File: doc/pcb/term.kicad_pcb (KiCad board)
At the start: 2 copper layers, 102.8 x 75.6 mm, 18 parts, among them U1 LM35-LP, U2 LM1117-3.3, U3 STM32F030F4Px, U4 CA56-12CGKWA

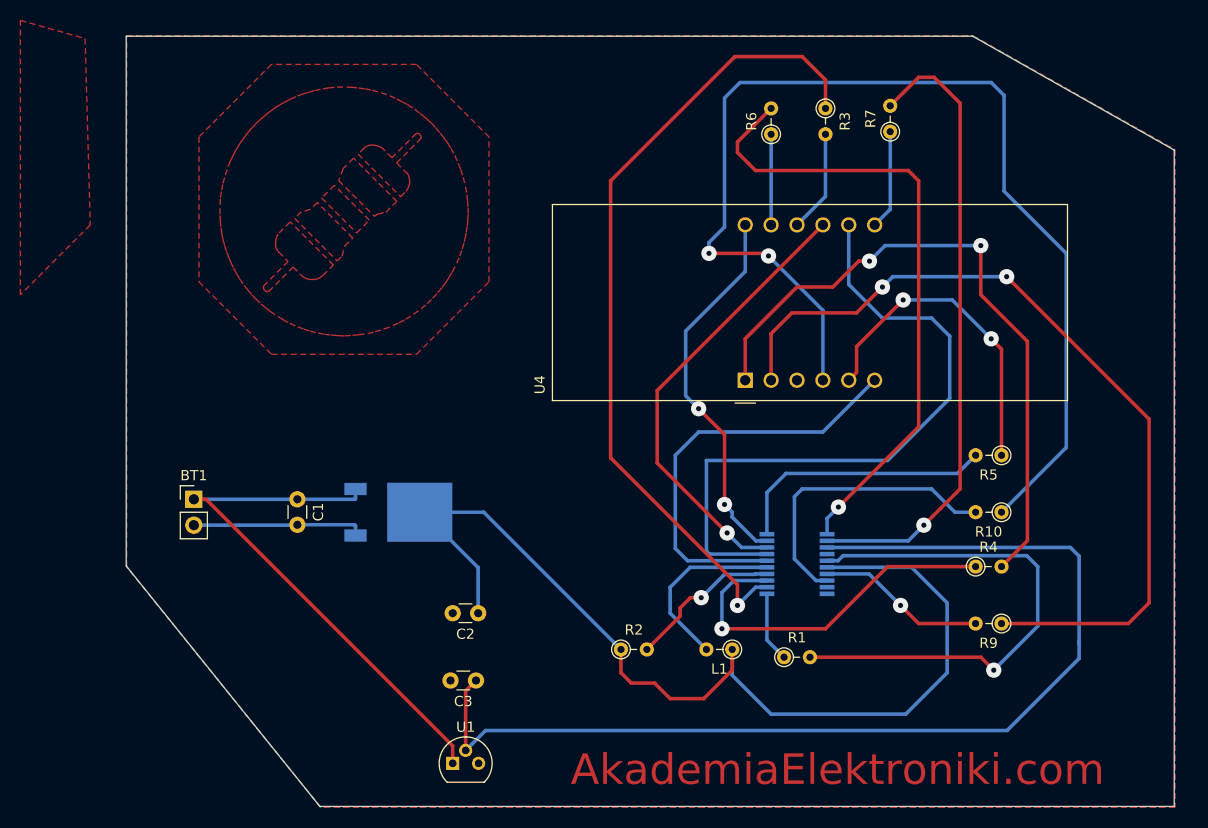
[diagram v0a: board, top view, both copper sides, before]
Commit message: new pcb as credit card
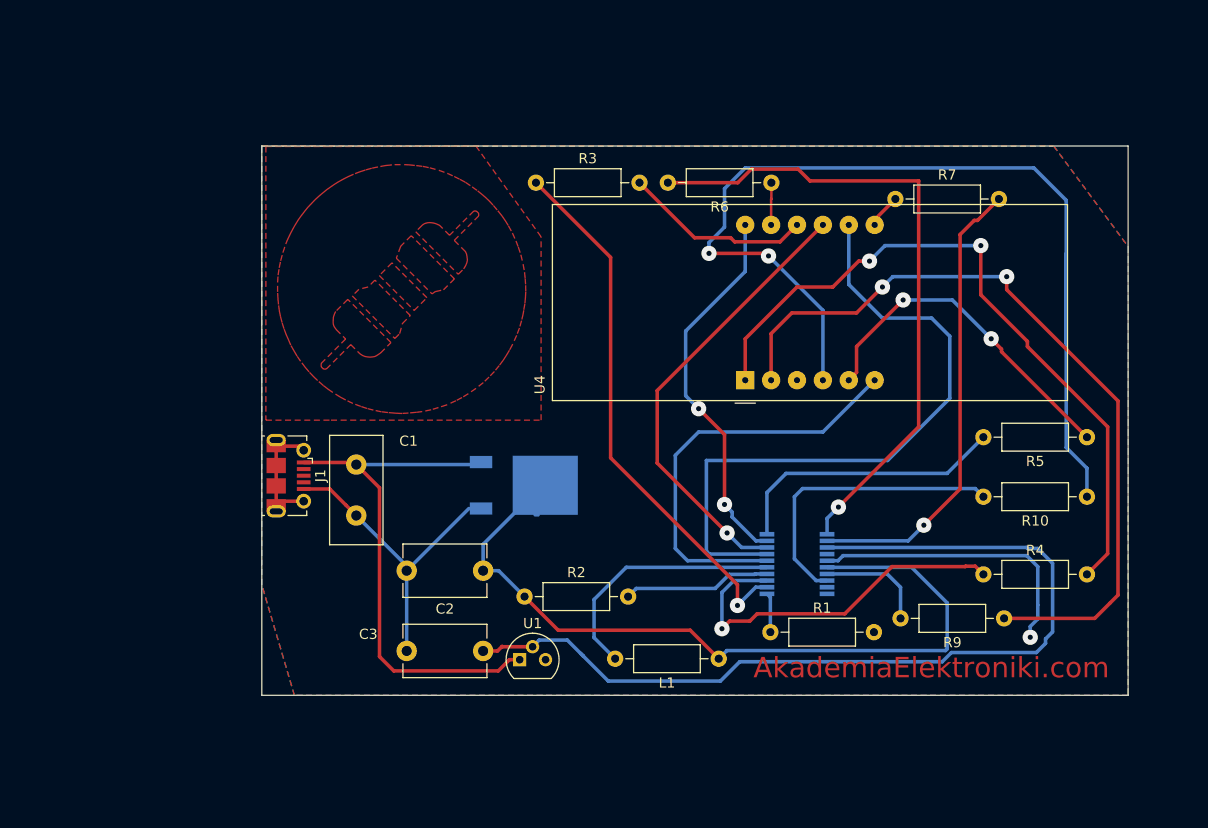
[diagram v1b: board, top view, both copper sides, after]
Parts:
- removed BT1: Battery, Connector_PinHeader_2.54mm:PinHeader_1x02_P2.54mm_Vertical
- added J1: USB_B_Micro, Connector_USB:USB_Micro-B_Molex-105017-0001, F.Cu at (138.3, 103.3)
- C1: footprint Capacitor_THT:C_Disc_D3.0mm_W1.6mm_P2.50mm -> Capacitor_THT:C_Disc_D10.5mm_W5.0mm_P5.00mm
- C2, C3: footprint Capacitor_THT:C_Disc_D3.0mm_W1.6mm_P2.50mm -> Capacitor_THT:C_Disc_D8.0mm_W5.0mm_P7.50mm
- L1, R1, R10, R2, R3, R4, R5, R6, R7, R9: footprint Resistor_THT:R_Axial_DIN0204_L3.6mm_D1.6mm_P2.54mm_Vertical -> Resistor_THT:R_Axial_DIN0207_L6.3mm_D2.5mm_P10.16mm_Horizontal
- moved R3 29.3 mm to (162.6, 74.6), turned to 0 degrees
- moved U2 12.6 mm to (161.4, 104.3)
- moved U1 12.1 mm to (161.0, 121.4)
- moved R2 10.8 mm to (161.5, 115.2)
- moved R5 8.57 mm to (216.7, 99.6)
- moved R10 8.52 mm to (216.7, 105.4)
- moved C1 6.71 mm to (145.0, 102.3)
- moved R7 6.62 mm to (197.9, 76.2), turned to 0 degrees
- moved R6 4.75 mm to (185.7, 74.6), turned to 180 degrees
- moved C2 4.20 mm to (157.4, 112.7)
- moved C3 2.98 mm to (157.4, 120.5)
- moved R1 2.80 mm to (185.6, 118.7)
- moved L1 1.61 mm to (180.5, 121.3)
- moved R4 1.08 mm to (206.5, 113.0)
- moved R9 0.57 mm to (208.5, 117.3)
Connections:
- net +9V renamed +5V
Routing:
- net Net-(R3-Pad1): track 80.3 -> 53.3 mm
- net Net-(C2-Pad1): track 102.2 -> 78.3 mm
- net Net-(R7-Pad2): track 62.1 -> 45.4 mm
- net Net-(C3-Pad1): track 106.6 -> 90.1 mm
- net Net-(J1-Pad6): track 0.00 -> 12.9 mm
- net GND: track 68.7 -> 58.3 mm
- net SF: track 10.0 -> 18.5 mm
- net Net-(L1-Pad2): track 17.9 -> 24.9 mm
- net SB: track 9.78 -> 3.38 mm
- net Net-(R9-Pad2): track 16.6 -> 10.8 mm, vias 1 -> 0
- net SD: track 83.1 -> 77.9 mm
- net SA: track 8.89 -> 4.51 mm
- net SC: track 110.9 -> 106.9 mm
- net SE: track 65.4 -> 69.2 mm
- net Net-(R1-Pad1): track 6.91 -> 3.90 mm
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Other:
- board size 102.8 x 75.6 mm -> 85 x 53.9 mm

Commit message: little details
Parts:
- R10: moved to B.Cu
- moved R7 1.96 mm to (198.4, 74.3)
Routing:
- net SG: track 33.8 -> 40.3 mm
- net SB: track 3.38 -> 5.49 mm
- net Net-(R7-Pad2): track 45.4 -> 47.3 mm
- net Net-(R6-Pad2): track 64.0 -> 65.6 mm
- net SE: track 69.2 -> 69.9 mm

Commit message: little pcb corrections
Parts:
- J1: footprint Connector_USB:USB_Micro-B_Molex-105017-0001 -> Connector_USB:USB_Micro-B_Molex_47346-0001
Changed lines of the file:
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@@
     (thickness 1.6)
     (drawings 8)
-    (tracks 233)
+    (tracks 232)
     (zones 0)
     (modules 18)
@@
     )
   )
-  (module Connector_USB:USB_Micro-B_Molex-105017-0001 (layer F.Cu)
+  (module Connector_USB:USB_Micro-B_Molex_47346-0001 (layer F.Cu)
     (at 138.35 103.35 270)
-    (descr http://www.molex.com/pdm_docs/sd/1050170001_sd.pdf)
-    (tags "Micro-USB SMD Typ-B")
+    (descr "Micro USB B receptable with flange, bottom-mount, SMD, right-angle (http://www.molex.com/pdm_docs/sd/473460001_sd.pdf)")
+    (tags "Micro B USB SMD")
     (attr smd)
-    (fp_text reference J1 (at 0 -3.1125 90) (layer F.SilkS)
-      (effects (font (size 1 1) (thickness 0.15)))
-    )
-    (fp_text value USB_B_Micro (at 5.95 -1.35 180) (layer F.Fab)
-      (effects (font (size 1 1) (thickness 0.15)))
-    )
-    (fp_text user "PCB Edge" (at 0 2.6875 90) (layer Dwgs.User)
-      (effects (font (size 0.5 0.5) (thickness 0.08)))
-    )
-    (fp_text user %R (at 0 0.8875 90) (layer F.Fab)
-      (effects (font (size 1 1) (thickness 0.15)))
-    )
-    (fp_line (start -4.4 3.64) (end 4.4 3.64) (layer F.CrtYd) (width 0.05))
-    (fp_line (start 4.4 -2.46) (end 4.4 3.64) (layer F.CrtYd) (width 0.05))
-    (fp_line (start -4.4 -2.46) (end 4.4 -2.46) (layer F.CrtYd) (width 0.05))
-    (fp_line (start -4.4 3.64) (end -4.4 -2.46) (layer F.CrtYd) (width 0.05))
-    (fp_line (start -3.9 -1.7625) (end -3.45 -1.7625) (layer F.SilkS) (width 0.12))
-    (fp_line (start -3.9 0.0875) (end -3.9 -1.7625) (layer F.SilkS) (width 0.12))
-    (fp_line (start 3.9 2.6375) (end 3.9 2.3875) (layer F.SilkS) (width 0.12))
-    (fp_line (start 3.75 3.3875) (end 3.75 -1.6125) (layer F.Fab) (width 0.1))
-    (fp_line (start -3 2.689204) (end 3 2.689204) (layer F.Fab) (width 0.1))
-    (fp_line (start -3.75 3.389204) (end 3.75 3.389204) (layer F.Fab) (width 0.1))
-    (fp_line (start -3.75 -1.6125) (end 3.75 -1.6125) (layer F.Fab) (width 0.1))
-    (fp_line (start -3.75 3.3875) (end -3.75 -1.6125) (layer F.Fab) (width 0.1))
-    (fp_line (start -3.9 2.6375) (end -3.9 2.3875) (layer F.SilkS) (width 0.12))
-    (fp_line (start 3.9 0.0875) (end 3.9 -1.7625) (layer F.SilkS) (width 0.12))
-    (fp_line (start 3.9 -1.7625) (end 3.45 -1.7625) (layer F.SilkS) (width 0.12))
-    (fp_line (start -1.7 -2.3125) (end -1.25 -2.3125) (layer F.SilkS) (width 0.12))
-    (fp_line (start -1.7 -2.3125) (end -1.7 -1.8625) (layer F.SilkS) (width 0.12))
-    (fp_line (start -1.3 -1.7125) (end -1.5 -1.9125) (layer F.Fab) (width 0.1))
-    (fp_line (start -1.1 -1.9125) (end -1.3 -1.7125) (layer F.Fab) (width 0.1))
-    (fp_line (start -1.5 -2.1225) (end -1.1 -2.1225) (layer F.Fab) (width 0.1))
-    (fp_line (start -1.5 -2.1225) (end -1.5 -1.9125) (layer F.Fab) (width 0.1))
-    (fp_line (start -1.1 -2.1225) (end -1.1 -1.9125) (layer F.Fab) (width 0.1))
-    (pad 6 smd rect (at 1 1.2375 270) (size 1.5 1.9) (layers F.Cu F.Paste F.Mask)
+    (fp_text reference J1 (at 0 -3.3 270) (layer F.SilkS)
+      (effects (font (size 1 1) (thickness 0.15)))
+    )
+    (fp_text value USB_B_Micro (at 0 4.6 270) (layer F.Fab)
+      (effects (font (size 1 1) (thickness 0.15)))
+    )
+    (fp_text user "PCB Edge" (at 0 2.67 270) (layer Dwgs.User)
+      (effects (font (size 0.4 0.4) (thickness 0.04)))
+    )
+    (fp_text user %R (at 0 1.2 90) (layer F.Fab)
+      (effects (font (size 1 1) (thickness 0.15)))
+    )
+    (fp_line (start 3.81 -1.71) (end 3.43 -1.71) (layer F.SilkS) (width 0.12))
+    (fp_line (start 4.6 3.9) (end -4.6 3.9) (layer F.CrtYd) (width 0.05))
+    (fp_line (start 4.6 -2.7) (end 4.6 3.9) (layer F.CrtYd) (width 0.05))
+    (fp_line (start -4.6 -2.7) (end 4.6 -2.7) (layer F.CrtYd) (width 0.05))
+    (fp_line (start -4.6 3.9) (end -4.6 -2.7) (layer F.CrtYd) (width 0.05))
+    (fp_line (start 3.75 3.35) (end -3.75 3.35) (layer F.Fab) (width 0.1))
+    (fp_line (start 3.75 -1.65) (end 3.75 3.35) (layer F.Fab) (width 0.1))
+    (fp_line (start -3.75 -1.65) (end 3.75 -1.65) (layer F.Fab) (width 0.1))
+    (fp_line (start -3.75 3.35) (end -3.75 -1.65) (layer F.Fab) (width 0.1))
+    (fp_line (start 3.81 2.34) (end 3.81 2.6) (layer F.SilkS) (width 0.12))
+    (fp_line (start 3.81 -1.71) (end 3.81 0.06) (layer F.SilkS) (width 0.12))
+    (fp_line (start -3.81 -1.71) (end -3.43 -1.71) (layer F.SilkS) (width 0.12))
+    (fp_line (start -3.81 0.06) (end -3.81 -1.71) (layer F.SilkS) (width 0.12))
+    (fp_line (start -3.81 2.6) (end -3.81 2.34) (layer F.SilkS) (width 0.12))
+    (fp_line (start -3.25 2.65) (end 3.25 2.65) (layer F.Fab) (width 0.1))
+    (pad 1 smd rect (at -1.3 -1.46 270) (size 0.45 1.38) (layers F.Cu F.Paste F.Mask)
+      (net 29 +5V))
+    (pad 2 smd rect (at -0.65 -1.46 270) (size 0.45 1.38) (layers F.Cu F.Paste F.Mask)
+      (net 31 "Net-(J1-Pad2)"))
+    (pad 3 smd rect (at 0 -1.46 270) (size 0.45 1.38) (layers F.Cu F.Paste F.Mask)
+      (net 33 "Net-(J1-Pad3)"))
+    (pad 4 smd rect (at 0.65 -1.46 270) (size 0.45 1.38) (layers F.Cu F.Paste F.Mask)
+      (net 32 "Net-(J1-Pad4)"))
+    (pad 5 smd rect (at 1.3 -1.46 270) (size 0.45 1.38) (layers F.Cu F.Paste F.Mask)
+      (net 1 GND))
+    (pad 6 smd rect (at -2.4625 -1.1 270) (size 1.475 2.1) (layers F.Cu F.Paste F.Mask)
       (net 30 "Net-(J1-Pad6)"))
-    (pad 6 thru_hole circle (at -2.5 -1.4625 270) (size 1.45 1.45) (drill 0.85) (layers *.Cu *.Mask)
+    (pad 6 smd rect (at 2.4625 -1.1 270) (size 1.475 2.1) (layers F.Cu F.Paste F.Mask)
       (net 30 "Net-(J1-Pad6)"))
-    (pad 2 smd rect (at -0.65 -1.4625 270) (size 0.4 1.35) (layers F.Cu F.Paste F.Mask)
-      (net 31 "Net-(J1-Pad2)"))
-    (pad 1 smd rect (at -1.3 -1.4625 270) (size 0.4 1.35) (layers F.Cu F.Paste F.Mask)
-      (net 29 +5V))
-    (pad 5 smd rect (at 1.3 -1.4625 270) (size 0.4 1.35) (layers F.Cu F.Paste F.Mask)
-      (net 1 GND))
-    (pad 4 smd rect (at 0.65 -1.4625 270) (size 0.4 1.35) (layers F.Cu F.Paste F.Mask)
-      (net 32 "Net-(J1-Pad4)"))
-    (pad 3 smd rect (at 0 -1.4625 270) (size 0.4 1.35) (layers F.Cu F.Paste F.Mask)
-      (net 33 "Net-(J1-Pad3)"))
-    (pad 6 thru_hole circle (at 2.5 -1.4625 270) (size 1.45 1.45) (drill 0.85) (layers *.Cu *.Mask)
+    (pad 6 smd rect (at -2.91 1.2 270) (size 2.375 1.9) (layers F.Cu F.Paste F.Mask)
       (net 30 "Net-(J1-Pad6)"))
-    (pad 6 smd rect (at -1 1.2375 270) (size 1.5 1.9) (layers F.Cu F.Paste F.Mask)
+    (pad 6 smd rect (at 2.91 1.2 270) (size 2.375 1.9) (layers F.Cu F.Paste F.Mask)
       (net 30 "Net-(J1-Pad6)"))
-    (pad 6 thru_hole oval (at -3.5 1.2375 90) (size 1.2 1.9) (drill oval 0.6 1.3) (layers *.Cu *.Mask)
+    (pad 6 smd rect (at -0.84 1.2 270) (size 1.175 1.9) (layers F.Cu F.Paste F.Mask)
       (net 30 "Net-(J1-Pad6)"))
-    (pad 6 thru_hole oval (at 3.5 1.2375 270) (size 1.2 1.9) (drill oval 0.6 1.3) (layers *.Cu *.Mask)
+    (pad 6 smd rect (at 0.84 1.2 270) (size 1.175 1.9) (layers F.Cu F.Paste F.Mask)
       (net 30 "Net-(J1-Pad6)"))
-    (pad 6 smd rect (at 2.9 1.2375 270) (size 1.2 1.9) (layers F.Cu F.Mask)
-      (net 30 "Net-(J1-Pad6)"))
-    (pad 6 smd rect (at -2.9 1.2375 270) (size 1.2 1.9) (layers F.Cu F.Mask)
-      (net 30 "Net-(J1-Pad6)"))
-    (model ${KISYS3DMOD}/Connector_USB.3dshapes/USB_Micro-B_Molex-105017-0001.wrl
+    (model ${KISYS3DMOD}/Connector_USB.3dshapes/USB_Micro-B_Molex_47346-0001.wrl
       (at (xyz 0 0 0))
       (scale (xyz 1 1 1))
@@
   (segment (start 207.264 89.916) (end 216.662 99.314) (width 0.35) (layer F.Cu) (net 10))
   (segment (start 185.928 78.486) (end 185.674 78.74) (width 0.35) (layer B.Cu) (net 11))
-  (segment (start 185.7 76.174) (end 185.7 74.6) (width 0.25) (layer F.Cu) (net 11))
-  (segment (start 185.674 78.74) (end 185.674 76.2) (width 0.25) (layer F.Cu) (net 11))
-  (segment (start 185.674 76.2) (end 185.7 76.174) (width 0.25) (layer F.Cu) (net 11))
+  (segment (start 185.7 78.714) (end 185.674 78.74) (width 0.35) (layer F.Cu) (net 11))
+  (segment (start 185.7 74.6) (end 185.7 78.714) (width 0.35) (layer F.Cu) (net 11))
   (segment (start 198.425 75.641) (end 198.425 74.325) (width 0.35) (layer F.Cu) (net 12))
   (segment (start 195.834 78.74) (end 195.834 78.232) (width 0.35) (layer F.Cu) (net 12))
